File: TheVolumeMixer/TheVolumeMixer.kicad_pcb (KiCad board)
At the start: 2 copper layers, 68 parts, among them J1 SJ1-3544, J10 Conn_01x01_Male, J11 Conn_01x01_Male, J2 Conn_01x01_Male, J3 Conn_01x01_Male, J4 SJ1-3544, J5 Conn_01x05, J6 Conn_01x01_Male, J7 Conn_01x01_Male, J8 Conn_01x01_Male, J9 Conn_01x01_Male, SW1 SW_Push, SW2 Rotary_Encoder_Switch, SW3 Rotary_Encoder_Switch, SW4 Rotary_Encoder_Switch, SW5 Rotary_Encoder_Switch, U1 TLC5947RHB, U2 ATSAMD21G18A-A, U3 AP2127K-3.3, U4 MAX9778, Y1 32.768kHz

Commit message: worked on PCB layout
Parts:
- moved J7 119.3 mm to (148.0, 64.0)
- moved J3 106.6 mm to (140.0, 64.0)
- moved J6 98.1 mm to (132.0, 64.0)
- moved J2 90.7 mm to (124.0, 64.0)
- moved SW2 87.8 mm to (123.0, 98.0)
- moved SW3 87.8 mm to (145.5, 98.0)
- moved SW4 87.8 mm to (168.0, 98.0)
- moved SW5 87.8 mm to (190.0, 98.0)
- moved J4 77.0 mm to (208.0, 121.0)
- moved R10 77.0 mm to (213.0, 108.0)
- moved R11 77.0 mm to (203.5, 108.0)
- moved R5 76.3 mm to (141.5, 78.5), turned to 270 degrees
- moved R4 75.3 mm to (171.0, 85.0), turned to 270 degrees
- moved SW1 74.0 mm to (153.0, 75.0)
- moved R3 73.6 mm to (165.0, 85.0), turned to 270 degrees
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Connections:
- SW3 pad A: /ROT3_A -> /ROT2_A
- SW3 pad B: /ROT3_B -> /ROT2_B
- SW3 pad S1: /ROT3_SW -> /ROT2_SW
- SW4 pad A: /ROT2_A -> /ROT3_A
- SW4 pad B: /ROT2_B -> /ROT3_B
- SW4 pad S1: /ROT2_SW -> /ROT3_SW

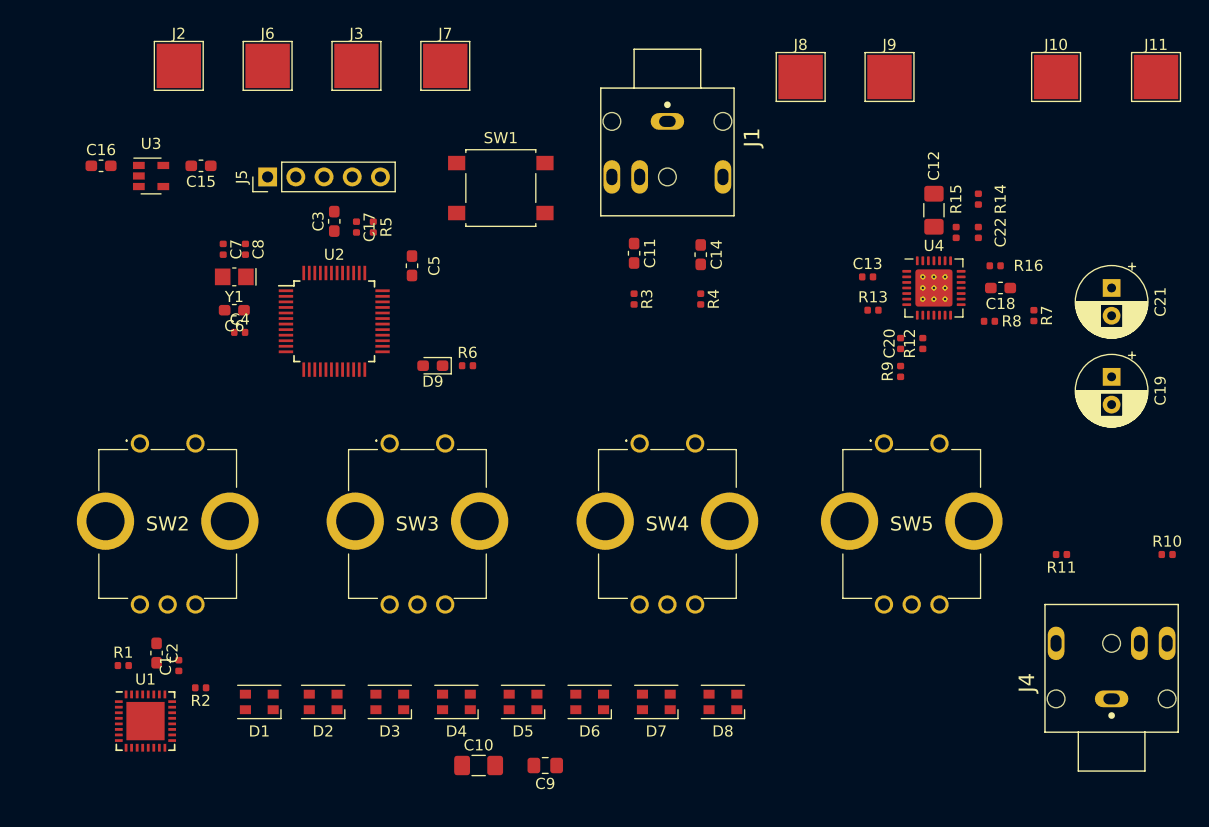
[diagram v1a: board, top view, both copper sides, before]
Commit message: finalized PCB layout. added 3D shapes for most components
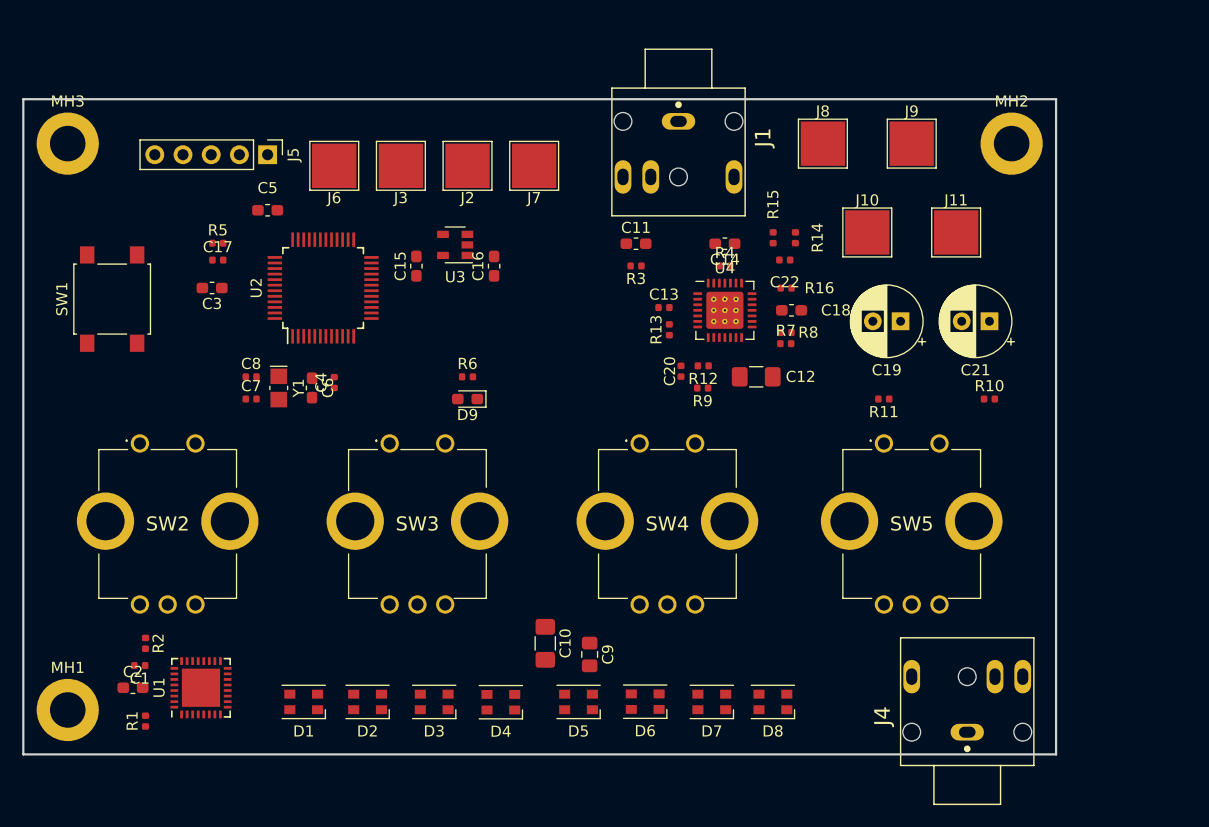
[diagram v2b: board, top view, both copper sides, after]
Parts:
- added MH1: MountingHole, MountingHole:MountingHole_3.2mm_M3_DIN965_Pad, F.Cu at (114.0, 122.0)
- added MH2: MountingHole, MountingHole:MountingHole_3.2mm_M3_DIN965_Pad, F.Cu at (199.0, 71.0)
- added MH3: MountingHole, MountingHole:MountingHole_3.2mm_M3_DIN965_Pad, F.Cu at (114.0, 71.0)
- moved C16 36.5 mm to (152.4, 82.0), turned to 90 degrees
- moved SW1 36.4 mm to (118.0, 85.0), turned to 90 degrees
- moved U3 28.1 mm to (148.9, 80.1), turned to 180 degrees
- moved J2 27.5 mm to (150.0, 73.0), turned to 180 degrees
- moved J11 22.8 mm to (194.0, 79.0)
- moved R7 22.5 mm to (178.7, 89.0), turned to 0 degrees
- moved J10 22.0 mm to (186.0, 79.0)
- moved C12 21.9 mm to (176.0, 92.0), turned to 180 degrees
- moved C15 21.4 mm to (145.4, 82.0), turned to 90 degrees
- moved R10 21.3 mm to (197.0, 94.0)
- moved R11 21.3 mm to (187.5, 94.0)
- moved C20 19.9 mm to (169.2, 91.5)
- moved R12 19.9 mm to (171.2, 91.0), turned to 180 degrees
- moved C19 19.6 mm to (189.0, 87.0), turned to 180 degrees
- moved C18 18.9 mm to (179.2, 86.0)
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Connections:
- net /USB_DM renamed /USB_D-
- net /USB_DP renamed /USB_D+
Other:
- board outline added: 93 x 59 mm
- net class Small added: clearance 0.1, trace_width 0.127, via_dia 0.8, via_drill 0.4
- rule trace_min: 0.2 -> 0.1

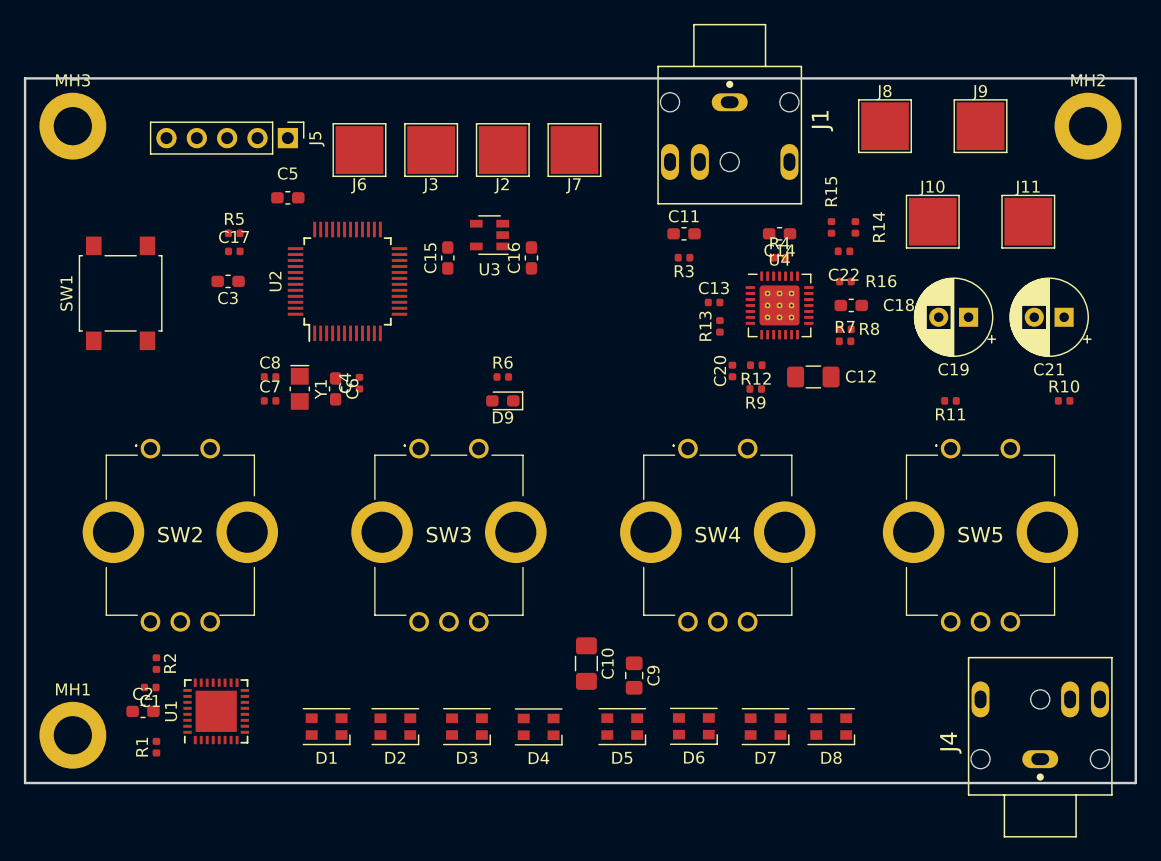
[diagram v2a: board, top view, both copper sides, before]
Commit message: PCB traces MCU, Volume Knobs, and Class D Amp routed
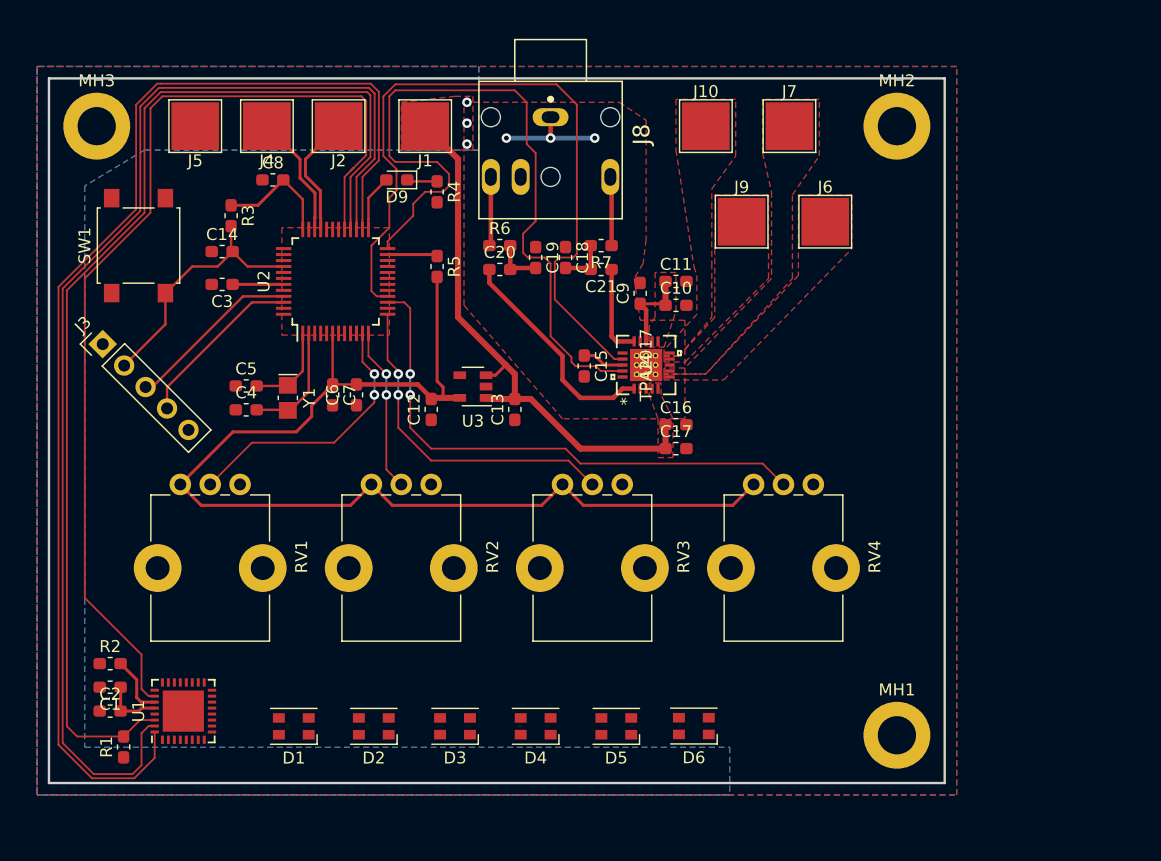
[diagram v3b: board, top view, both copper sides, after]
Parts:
- removed the C12 at (176.0, 92.0)
- removed C22: 0.047uF, Capacitor_SMD:C_0402_1005Metric
- removed the C7 at (130.5, 94.0)
- removed D7, D8: LED_RGBA, LED_SMD:LED_Cree-PLCC4_3.2x2.8mm_CCW
- removed J11: Conn_01x01_Male, TestPoint:TestPoint_Pad_4.0x4.0mm
- removed the J4 at (195.0, 124.0)
- removed the J8 at (182.0, 71.0)
- removed R10, R11: 10k, Resistor_SMD:R_0402_1005Metric
- removed R12, R15: 33.2k, Resistor_SMD:R_0402_1005Metric
- removed R13, R16: 15k, Resistor_SMD:R_0402_1005Metric
- removed R14, R9: 27.4k, Resistor_SMD:R_0402_1005Metric
- removed R8: 47k, Resistor_SMD:R_0402_1005Metric
- removed SW2, SW3, SW4, SW5: Rotary_Encoder_Switch, PEC11R-4215K-S0012 Rotary Encoder:PEC11R4220KS0024
- added C15: 0.1uF, Capacitor_SMD:C_0603_1608Metric_Pad1.05x0.95mm_HandSolder, F.Cu at (156.8, 91.1)
- added C5: 22pF, Capacitor_SMD:C_0603_1608Metric_Pad1.05x0.95mm_HandSolder, F.Cu at (128.5, 92.8)
- added J6: Conn_01x01_Male, TestPoint:TestPoint_Pad_4.0x4.0mm, F.Cu at (177.0, 79.0)
- added J7: Conn_01x01_Male, TestPoint:TestPoint_Pad_4.0x4.0mm, F.Cu at (174.0, 71.0)
- added RV1: R_POT_US, Potentiometer - PTV09A-4020F-B203:Potentiometer_Bourns_PTV09A-1_Single_Vertical, F.Cu at (123.0, 101.0)
- added RV2: R_POT_US, Potentiometer - PTV09A-4020F-B203:Potentiometer_Bourns_PTV09A-1_Single_Vertical, F.Cu at (139.0, 101.0)
- added RV3: R_POT_US, Potentiometer - PTV09A-4020F-B203:Potentiometer_Bourns_PTV09A-1_Single_Vertical, F.Cu at (155.0, 101.0)
- added RV4: R_POT_US, Potentiometer - PTV09A-4020F-B203:Potentiometer_Bourns_PTV09A-1_Single_Vertical, F.Cu at (171.0, 101.0)
- C1: footprint Capacitor_SMD:C_0402_1005Metric -> Capacitor_SMD:C_0603_1608Metric_Pad1.05x0.95mm_HandSolder
- C10: value 100uF -> 0.1uF; footprint Capacitor_SMD:C_1206_3216Metric_Pad1.42x1.75mm_HandSolder -> Capacitor_SMD:C_0603_1608Metric_Pad1.05x0.95mm_HandSolder
- C11: value 0.68uF -> 1uF
- C13, C17: value 0.1uF -> 1uF; footprint Capacitor_SMD:C_0402_1005Metric -> Capacitor_SMD:C_0603_1608Metric_Pad1.05x0.95mm_HandSolder
- C14: value 0.68uF -> 0.1uF
- C16: value 1uF -> 0.1uF
- C18: value 1uF -> 0.047uF
- C19: value 220uF -> 0.047uF; footprint Capacitor_THT:CP_Radial_D6.3mm_P2.50mm -> Capacitor_SMD:C_0603_1608Metric_Pad1.05x0.95mm_HandSolder
- C20: value 0.047uF -> 1uF; footprint Capacitor_SMD:C_0402_1005Metric -> Capacitor_SMD:C_0603_1608Metric_Pad1.05x0.95mm_HandSolder
- C21: value 220uF -> 1uF; footprint Capacitor_THT:CP_Radial_D6.3mm_P2.50mm -> Capacitor_SMD:C_0603_1608Metric_Pad1.05x0.95mm_HandSolder
- C4: value 0.1uF -> 22pF; footprint Capacitor_SMD:C_0402_1005Metric -> Capacitor_SMD:C_0603_1608Metric_Pad1.05x0.95mm_HandSolder
- C6: renamed from C5; value 1uF -> 0.1uF
- C8: value 22pF -> 0.1uF; footprint Capacitor_SMD:C_0402_1005Metric -> Capacitor_SMD:C_0603_1608Metric_Pad1.05x0.95mm_HandSolder
- C9: value 10uF -> 0.1uF; footprint Capacitor_SMD:C_0805_2012Metric_Pad1.15x1.40mm_HandSolder -> Capacitor_SMD:C_0603_1608Metric_Pad1.05x0.95mm_HandSolder
- R1, R2: footprint Resistor_SMD:R_0402_1005Metric -> Resistor_SMD:R_0603_1608Metric_Pad1.05x0.95mm_HandSolder
- R3: value 15k -> 10k; footprint Resistor_SMD:R_0402_1005Metric -> Resistor_SMD:R_0603_1608Metric_Pad1.05x0.95mm_HandSolder
- R4: value 15k -> 2.2k; footprint Resistor_SMD:R_0402_1005Metric -> Resistor_SMD:R_0603_1608Metric_Pad1.05x0.95mm_HandSolder
- R5: value 10k -> 100k; footprint Resistor_SMD:R_0402_1005Metric -> Resistor_SMD:R_0603_1608Metric_Pad1.05x0.95mm_HandSolder
- R6: value 2.2k -> 100; footprint Resistor_SMD:R_0402_1005Metric -> Resistor_SMD:R_0603_1608Metric_Pad1.05x0.95mm_HandSolder
- R7: value 680k -> 100; footprint Resistor_SMD:R_0402_1005Metric -> Resistor_SMD:R_0603_1608Metric_Pad1.05x0.95mm_HandSolder
- U4: value MAX9778 -> TPA2017; footprint Package_DFN_QFN:QFN-28-1EP_5x5mm_P0.5mm_EP3.35x3.35mm_ThermalVias -> footprints:TPA2017D2RTJR
- moved MH1 69.0 mm to (183.0, 122.0)
- moved C14 46.7 mm to (126.5, 81.5), turned to 0 degrees
- moved C17 40.5 mm to (164.5, 98.0)
- moved C21 39.0 mm to (158.2, 83.0)
- moved R3 38.1 mm to (127.2, 78.5), turned to 270 degrees
- moved C19 36.6 mm to (152.8, 82.0), turned to 270 degrees
- moved C9 32.0 mm to (161.5, 85.0), turned to 90 degrees
- moved J5 31.8 mm to (124.2, 71.0)
- moved C10 30.9 mm to (164.5, 86.0), turned to 0 degrees
- moved R4 29.2 mm to (144.5, 76.5), turned to 270 degrees
- moved C18 24.3 mm to (155.2, 82.0), turned to 270 degrees
- moved J3 23.2 mm to (116.5, 89.2), turned to 45 degrees
- moved R7 21.9 mm to (158.2, 81.0), turned to 180 degrees
- moved J9 21.5 mm to (170.0, 79.0)
- moved C20 21.2 mm to (149.8, 83.0), turned to 0 degrees
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- renumbered C15 to C12, C6 to C7, J2 to J1, J3 to J2, J5 to J3, J6 to J4, J7 to J5, J1 to J8
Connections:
- C10 pad 1: GND -> +5V
- C10 pad 2: +5V -> GND
- C11 pad 1: Net-(C11-Pad1) -> +5V
- C11 pad 2: Net-(C11-Pad2) -> GND
- C14 pad 1: Net-(C14-Pad1) -> GND
- C14 pad 2: Net-(C14-Pad2) -> /RESET'
- C16 pad 1: GND -> +5V
- C16 pad 2: +5V -> GND
- C17 pad 1: GND -> +5V
- C17 pad 2: /RESET' -> GND
- C18 pad 1: GND -> GNDA
- C19 pad 1: /OUTL+ -> GNDA
- C20 pad 1: /GAINLB -> /INL+
- C20 pad 2: Net-(C20-Pad2) -> Net-(C19-Pad2)
- C21 pad 1: /OUTR+ -> /INR+
- C21 pad 2: Net-(C21-Pad2) -> Net-(C18-Pad2)
- C4 pad 2: +3V3 -> Net-(C4-Pad2)
- C8 pad 2: Net-(C8-Pad2) -> +3V3
- C9 pad 1: GND -> +5V
- C9 pad 2: +5V -> GND
- D9 pad 2: /D13_LED -> /D2_LED
- J10 pad 1: /OUTL- -> /OUTR+
- J3 pad 2: /SWCLK -> /RESET'
- J3 pad 3: /SWDIO -> /SWCLK
- J3 pad 4: /RESET' -> /SWDIO
- J8 pad 1: GND -> GNDA
- J8 pad 2: Net-(C11-Pad1) -> Net-(J8-Pad2)
- J8 pad 3: Net-(C14-Pad1) -> Net-(J8-Pad3)
- J9 pad 1: /OUTR+ -> /OUTR-
- R3 pad 1: Net-(C11-Pad2) -> +3V3
- R3 pad 2: /INL1 -> /RESET'
- R4 pad 1: Net-(C14-Pad2) -> Net-(D9-Pad1)
- R4 pad 2: /INR1 -> GND
- R5 pad 1: +3V3 -> /EN
- R5 pad 2: /RESET' -> +3V3
- R6 pad 1: Net-(D9-Pad1) -> Net-(J8-Pad2)
- R6 pad 2: GND -> Net-(C19-Pad2)
- R7 pad 1: +5V -> Net-(J8-Pad3)
- R7 pad 2: /TN -> Net-(C18-Pad2)
- U2 pad 1: Net-(C8-Pad2) -> Net-(C5-Pad2)
- U2 pad 10: /LED_OFF -> Net-(U2-Pad10)
- U2 pad 11: /LED_LATCH -> /VOL1
- U2 pad 12: /LED_CLK -> /VOL2
- U2 pad 13: /LED_DATA -> /VOL3
- U2 pad 15: /ROT1_A -> /VOL4
- U2 pad 16: /ROT1_B -> /SP_GC1
- U2 pad 19: /GAINA' -> Net-(U2-Pad19)
- U2 pad 2: Net-(C7-Pad2) -> Net-(C4-Pad2)
- U2 pad 20: /HPS_EN -> Net-(U2-Pad20)
- U2 pad 21: /ROT1_SW -> Net-(U2-Pad21)
- U2 pad 23: /ROT2_A -> /EN
- U2 pad 24: /D13_LED -> /SP_GC2
- U2 pad 25: /ROT2_B -> /D2_LED
- U2 pad 26: /ROT2_SW -> /LED_DATA
- U2 pad 27: /ROT3_A -> /LED_CLK
- U2 pad 28: /ROT3_B -> /LED_OFF
- U2 pad 29: /ROT3_SW -> /LED_LATCH
- U2 pad 30: /ROT4_A -> Net-(U2-Pad30)
- U2 pad 31: /ROT4_B -> Net-(U2-Pad31)
- U2 pad 32: /ROT4_SW -> Net-(U2-Pad32)
- U2 pad 47: /SHDN' -> Net-(U2-Pad47)
- U2 pad 7: /IN1' -> Net-(U2-Pad7)
- U2 pad 8: /MUTE -> Net-(U2-Pad8)
- U4 pad 1: /MUTE -> /INL+
- U4 pad 10: /OUTL+ -> /OUTR+
- U4 pad 12: /OUTL- -> +5V
- U4 pad 13: GND -> +5V
- U4 pad 14: /SHDN' -> GNDA
- U4 pad 15: /GAINA' -> /INR+
- U4 pad 16: Net-(R8-Pad1) -> GND
- U4 pad 17: Net-(C18-Pad2) -> /SP_GC1
- U4 pad 18: GND -> /EN
- U4 pad 19: /INR1 -> /SP_GC2
- U4 pad 2: /HPS_EN -> GNDA
- U4 pad 21: /GAINRA -> (no net)
- U4 pad 3: +5V -> GNDA
- U4 pad 5: /INL1 -> +5V
- U4 pad 6: GND -> /OUTL+
- U4 pad 7: /GAINLA -> /OUTL-
- U4 pad 8: /GAINLB -> GND
- U4 pad 9: GND -> /OUTR-
- Y1 pad 1: Net-(C8-Pad2) -> Net-(C5-Pad2)
- Y1 pad 2: Net-(C7-Pad2) -> Net-(C4-Pad2)
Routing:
- net +3V3: track 0.00 -> 105.2 mm
- net /LED_DATA: track 0.00 -> 101.8 mm
- net /LED_CLK: track 0.00 -> 100.5 mm
- net /LED_OFF: track 0.00 -> 94.2 mm
- net /LED_LATCH: track 0.00 -> 84.7 mm
- net /SP_GC1: track 0.00 -> 62.0 mm
- net /SP_GC2: track 0.00 -> 61.6 mm
- net +5V: track 0.00 -> 59.2 mm, vias 0 -> 3
- net /VOL4: track 0.00 -> 45.3 mm, vias 0 -> 2
- net /VOL3: track 0.00 -> 28.1 mm, vias 0 -> 2
- net /VOL1: track 0.00 -> 22.8 mm, vias 0 -> 2
- net /RESET': track 0.00 -> 21.4 mm
- net /INL+: track 0.00 -> 18.7 mm
- net /SWCLK: track 0.00 -> 14.7 mm
- net /SWDIO: track 0.00 -> 14.5 mm
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- added copper zone on B.Cu, net (none)
- added copper zone on F.Cu, net +3V3
- added copper zone on B.Cu, net +5V
- added copper zone on F.Cu, net +5V
- added copper zone on F.Cu, net /OUTL+
- added copper zone on F.Cu, net /OUTL-
- added copper zone on F.Cu, net /OUTR+
- added copper zone on F.Cu, net /OUTR-
- added copper zone on F.Cu, net GND
- added copper zone on F.Cu, net GNDA
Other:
- board size 93 x 59 mm -> 75 x 59 mm
- rule trace_min: 0.1 -> 0.127

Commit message: rev 1 PCB complete -- not finished
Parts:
- moved J6 9.71 mm to (182.5, 87.0)
- moved J7 9.71 mm to (179.5, 79.0)
- moved C1 2.00 mm to (117.1, 116.0)
- moved C2 2.00 mm to (117.1, 118.0)
- moved R1 2.00 mm to (118.2, 121.0)
- moved R2 2.00 mm to (117.1, 114.0)
- moved U1 2.00 mm to (123.2, 118.0)
- moved D6 1.00 mm to (167.0, 121.2)
- moved D5 0.60 mm to (160.1, 121.2)
- moved R4 0.50 mm to (144.0, 76.5)
- moved D4 0.45 mm to (153.2, 121.2)
- moved D3 0.30 mm to (146.3, 121.2)
- moved D2 0.20 mm to (139.4, 121.3)
- renumbered D9 to D7
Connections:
- net /D7_B renamed Net-(U1-Pad21)
- net /D8_B renamed Net-(U1-Pad24)
- net /D8_G renamed Net-(U1-Pad23)
- net /D8_R renamed Net-(U1-Pad22)
- D1 pad 3: (no net) -> /D1_B
- D2 pad 1: /D5_R -> /D2_R
- D2 pad 2: /D5_G -> /D2_G
- D2 pad 3: (no net) -> /D2_B
- D3 pad 1: /D2_R -> /D3_R
- D3 pad 2: /D2_G -> /D3_G
- D3 pad 3: (no net) -> /D3_B
- D4 pad 1: /D6_R -> /D4_R
- D4 pad 2: /D6_G -> /D4_G
- D4 pad 3: (no net) -> /D4_B
- D5 pad 1: /D3_R -> /D5_R
- D5 pad 2: /D3_G -> /D5_G
- D5 pad 3: (no net) -> /D5_B
- D6 pad 1: /D7_R -> /D6_R
- D6 pad 2: /D7_G -> /D6_G
- D6 pad 3: (no net) -> /D6_B
- U1 pad 1: /D1_R -> /D6_R
- U1 pad 10: /D4_R -> /D1_G
- U1 pad 11: /D4_G -> /D2_B
- U1 pad 12: /D4_B -> /D2_G
- U1 pad 13: /D5_R -> /D3_B
- U1 pad 14: /D5_G -> /D3_G
- U1 pad 15: /D5_B -> /D4_B
- U1 pad 16: /D6_R -> /D4_G
- U1 pad 17: /D6_G -> /D5_B
- U1 pad 18: /D6_B -> /D5_G
- U1 pad 19: /D7_R -> /D6_B
- U1 pad 2: /D1_G -> /D5_R
- U1 pad 20: /D7_G -> /D6_G
- U1 pad 3: /D1_B -> /D4_R
- U1 pad 4: /D2_R -> /D3_R
- U1 pad 5: /D2_G -> /D2_R
- U1 pad 6: /D2_B -> /D1_R
- U1 pad 7: /D3_R -> Net-(U1-Pad7)
- U1 pad 8: /D3_G -> Net-(U1-Pad8)
- U1 pad 9: /D3_B -> /D1_B
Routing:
- net /EN: track 7.79 -> 67.2 mm
- net /D6_R: track 0.00 -> 51.9 mm
- net /D6_G: track 0.00 -> 49.6 mm
- net /D6_B: track 0.00 -> 46.1 mm
- net /D5_R: track 0.00 -> 44.1 mm
- net /D5_G: track 0.00 -> 40.8 mm
- net /D4_R: track 0.00 -> 36.2 mm
- net /D5_B: track 0.00 -> 35.9 mm
- net /D4_G: track 0.00 -> 30.6 mm
- net /D3_R: track 0.00 -> 28.3 mm
- net /D4_B: track 0.00 -> 27.9 mm
- net /D3_G: track 0.00 -> 23.3 mm
- net /D3_B: track 0.00 -> 20.6 mm
- net /D2_R: track 0.00 -> 20.5 mm
- net +5V: track 59.2 -> 75.5 mm, vias 3 -> 10
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- added copper zone on B.Cu, net GND
- removed copper zone on B.Cu, net (none)
